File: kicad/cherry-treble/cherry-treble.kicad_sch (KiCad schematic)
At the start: 103 parts

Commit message: Pick compatible PCB components for cherry trebble
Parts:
- Conn1: footprint Connector_Multicomp:Multicomp_MC9A12-2634_2x13_P2.54mm_Vertical -> Connector_IDC:IDC-Header_2x13_P2.54mm_Vertical
- R0, R1, R2, R3, R4, R5: footprint Resistor_SMD:R_1206_3216Metric_Pad1.42x1.75mm_HandSolder -> Resistor_SMD:R_1206_3216Metric_Pad1.30x1.75mm_HandSolder
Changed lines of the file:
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@@
       (effects (font (size 1.27 1.27)) (justify left))
     )
-    (property "Footprint" "Resistor_SMD:R_1206_3216Metric_Pad1.42x1.75mm_HandSolder" (id 2) (at 153.67 155.448 90)
+    (property "Footprint" "Resistor_SMD:R_1206_3216Metric_Pad1.30x1.75mm_HandSolder" (id 2) (at 153.67 155.448 90)
       (effects (font (size 1.27 1.27)) hide)
     )
@@
       (effects (font (size 1.27 1.27)) (justify left))
     )
-    (property "Footprint" "Resistor_SMD:R_1206_3216Metric_Pad1.42x1.75mm_HandSolder" (id 2) (at 153.67 133.858 90)
+    (property "Footprint" "Resistor_SMD:R_1206_3216Metric_Pad1.30x1.75mm_HandSolder" (id 2) (at 153.67 133.858 90)
       (effects (font (size 1.27 1.27)) hide)
     )
@@
       (effects (font (size 1.27 1.27)) (justify left))
     )
-    (property "Footprint" "Resistor_SMD:R_1206_3216Metric_Pad1.42x1.75mm_HandSolder" (id 2) (at 153.67 112.268 90)
+    (property "Footprint" "Resistor_SMD:R_1206_3216Metric_Pad1.30x1.75mm_HandSolder" (id 2) (at 153.67 112.268 90)
       (effects (font (size 1.27 1.27)) hide)
     )
@@
     (property "Reference" "Conn1" (id 0) (at 190.5 17.3482 0))
     (property "Value" "Conn_02x13_Odd_Even" (id 1) (at 190.5 19.6596 0))
-    (property "Footprint" "Connector_Multicomp:Multicomp_MC9A12-2634_2x13_P2.54mm_Vertical" (id 2) (at 189.23 38.1 0)
+    (property "Footprint" "Connector_IDC:IDC-Header_2x13_P2.54mm_Vertical" (id 2) (at 189.23 38.1 0)
       (effects (font (size 1.27 1.27)) hide)
     )
@@
       (effects (font (size 1.27 1.27)) (justify left))
     )
-    (property "Footprint" "Resistor_SMD:R_1206_3216Metric_Pad1.42x1.75mm_HandSolder" (id 2) (at 153.67 90.678 90)
+    (property "Footprint" "Resistor_SMD:R_1206_3216Metric_Pad1.30x1.75mm_HandSolder" (id 2) (at 153.67 90.678 90)
       (effects (font (size 1.27 1.27)) hide)
     )
@@
       (effects (font (size 1.27 1.27)) (justify left))
     )
-    (property "Footprint" "Resistor_SMD:R_1206_3216Metric_Pad1.42x1.75mm_HandSolder" (id 2) (at 153.67 69.088 90)
+    (property "Footprint" "Resistor_SMD:R_1206_3216Metric_Pad1.30x1.75mm_HandSolder" (id 2) (at 153.67 69.088 90)
       (effects (font (size 1.27 1.27)) hide)
     )
@@
       (effects (font (size 1.27 1.27)) (justify left))
     )
-    (property "Footprint" "Resistor_SMD:R_1206_3216Metric_Pad1.42x1.75mm_HandSolder" (id 2) (at 153.67 47.498 90)
+    (property "Footprint" "Resistor_SMD:R_1206_3216Metric_Pad1.30x1.75mm_HandSolder" (id 2) (at 153.67 47.498 90)
       (effects (font (size 1.27 1.27)) hide)
     )
@@
     )
     (path "/9e3b6ef3-52a8-4dd9-a8f4-b7171c5fee3c"
-      (reference "Conn1") (unit 1) (value "Conn_02x13_Odd_Even") (footprint "Connector_Multicomp:Multicomp_MC9A12-2634_2x13_P2.54mm_Vertical")
+      (reference "Conn1") (unit 1) (value "Conn_02x13_Odd_Even") (footprint "Connector_IDC:IDC-Header_2x13_P2.54mm_Vertical")
     )
     (path "/97178bdc-fdcc-45db-99b3-0df4ecddfa55"
@@
     )
     (path "/cfce948b-9f72-4e81-a12b-89c726c6fcef"
-      (reference "R0") (unit 1) (value "10k") (footprint "Resistor_SMD:R_1206_3216Metric_Pad1.42x1.75mm_HandSolder")
+      (reference "R0") (unit 1) (value "10k") (footprint "Resistor_SMD:R_1206_3216Metric_Pad1.30x1.75mm_HandSolder")
     )
     (path "/bff3b85d-eb38-420c-9f5c-44f931425e43"
-      (reference "R1") (unit 1) (value "10k") (footprint "Resistor_SMD:R_1206_3216Metric_Pad1.42x1.75mm_HandSolder")
+      (reference "R1") (unit 1) (value "10k") (footprint "Resistor_SMD:R_1206_3216Metric_Pad1.30x1.75mm_HandSolder")
     )
     (path "/b5a7ad3d-c26d-4413-83db-9bfba22fa6f0"
-      (reference "R2") (unit 1) (value "10k") (footprint "Resistor_SMD:R_1206_3216Metric_Pad1.42x1.75mm_HandSolder")
+      (reference "R2") (unit 1) (value "10k") (footprint "Resistor_SMD:R_1206_3216Metric_Pad1.30x1.75mm_HandSolder")
     )
     (path "/986371c7-5271-475e-9c30-54695843300e"
-      (reference "R3") (unit 1) (value "10k") (footprint "Resistor_SMD:R_1206_3216Metric_Pad1.42x1.75mm_HandSolder")
+      (reference "R3") (unit 1) (value "10k") (footprint "Resistor_SMD:R_1206_3216Metric_Pad1.30x1.75mm_HandSolder")
     )
     (path "/5e9c7ff3-fbe3-4ba5-b51a-22b9f0fd8c94"
-      (reference "R4") (unit 1) (value "10k") (footprint "Resistor_SMD:R_1206_3216Metric_Pad1.42x1.75mm_HandSolder")
+      (reference "R4") (unit 1) (value "10k") (footprint "Resistor_SMD:R_1206_3216Metric_Pad1.30x1.75mm_HandSolder")
     )
     (path "/3ff8e6a9-719c-4bfc-af0b-9e00ac7758b8"
-      (reference "R5") (unit 1) (value "10k") (footprint "Resistor_SMD:R_1206_3216Metric_Pad1.42x1.75mm_HandSolder")
+      (reference "R5") (unit 1) (value "10k") (footprint "Resistor_SMD:R_1206_3216Metric_Pad1.30x1.75mm_HandSolder")
     )
     (path "/284fe915-29d9-4b8c-b528-5698bc79fdd4"

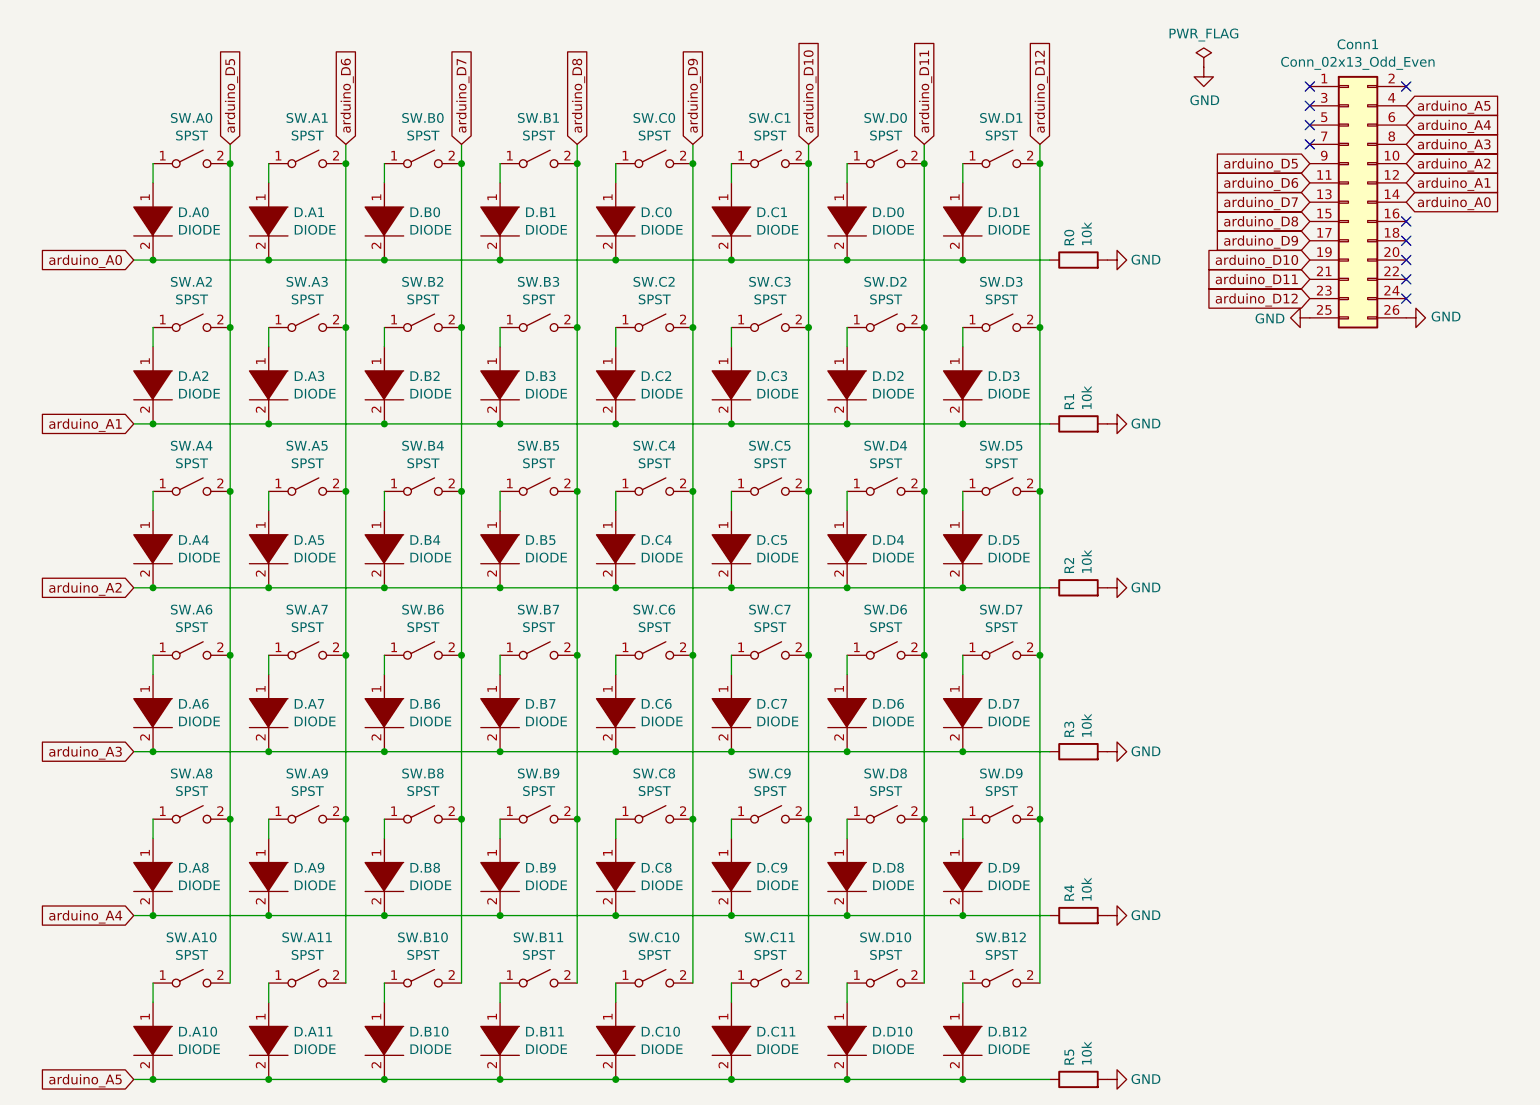
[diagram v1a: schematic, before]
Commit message: Update wiring schematic for cherry treble
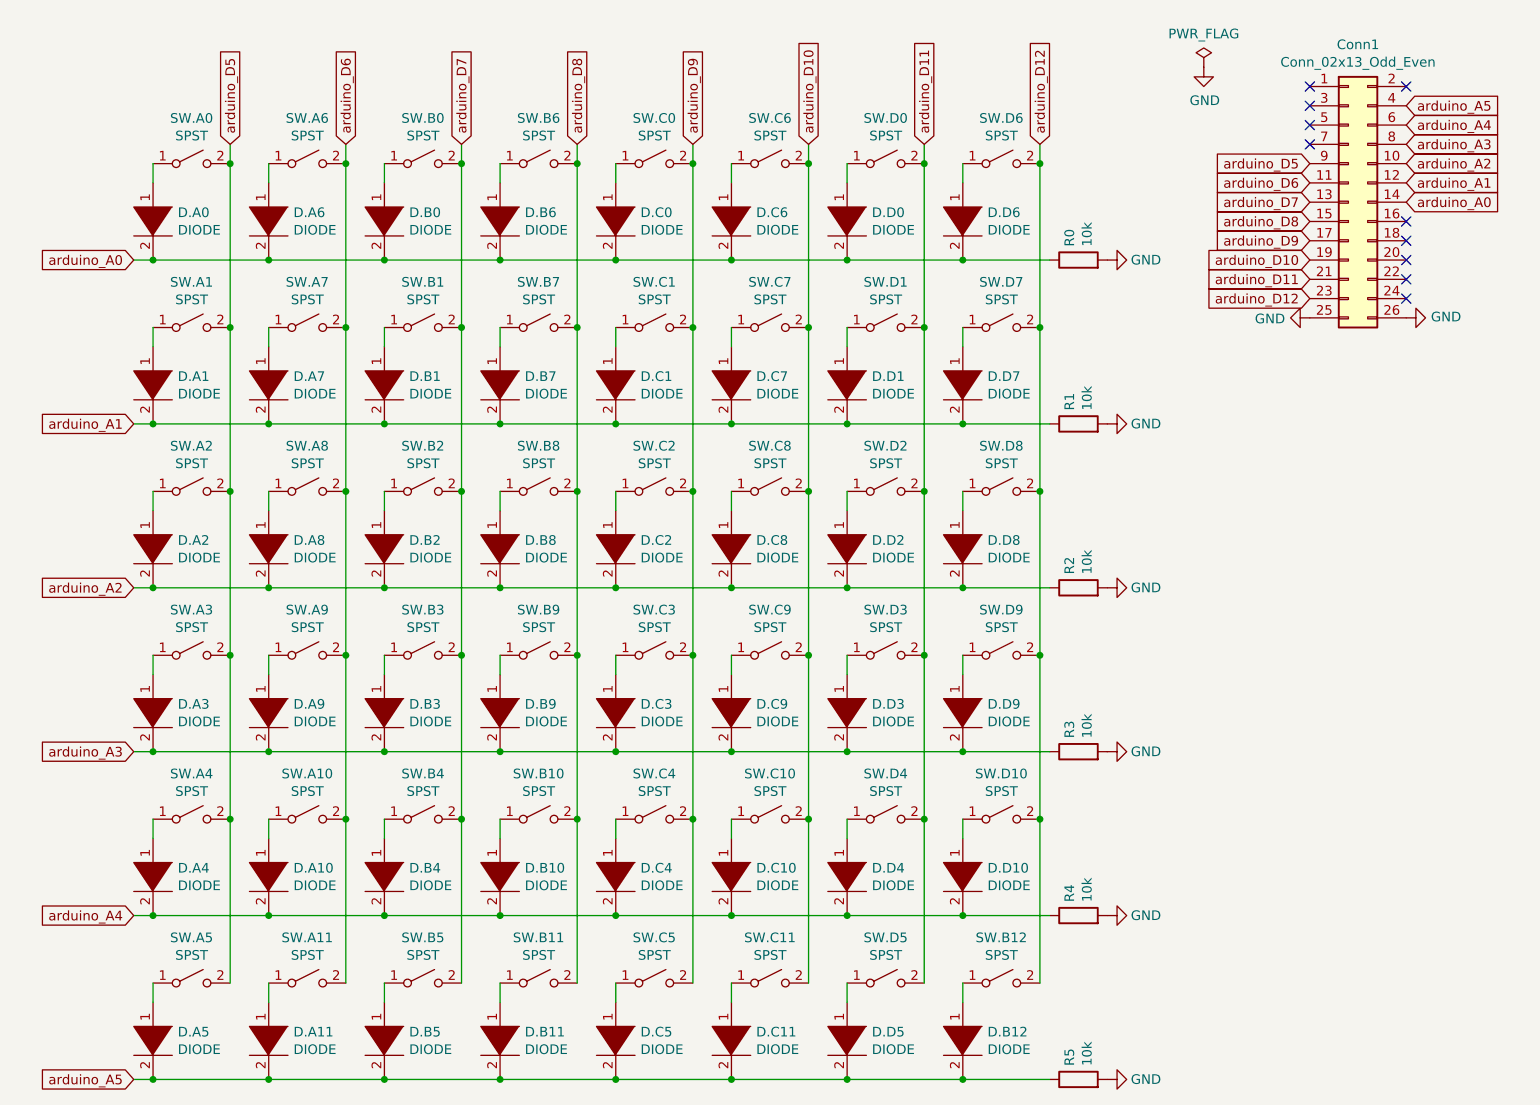
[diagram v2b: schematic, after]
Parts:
- renumbered D.A2 to D.A1, D.A9 to D.A10, D.A4 to D.A2, D.A6 to D.A3, D.A8 to D.A4, D.A10 to D.A5, D.A1 to D.A6, D.A3 to D.A7, D.A5 to D.A8, D.A7 to D.A9, D.B2 to D.B1, D.B9 to D.B10, D.B4 to D.B2, D.B6 to D.B3, D.B8 to D.B4, D.B10 to D.B5, D.B1 to D.B6, D.B3 to D.B7, D.B5 to D.B8, D.B7 to D.B9, D.C2 to D.C1, D.C9 to D.C10, D.C4 to D.C2, D.C6 to D.C3, D.C8 to D.C4, D.C10 to D.C5, D.C1 to D.C6, D.C3 to D.C7, D.C5 to D.C8, D.C7 to D.C9, D.D2 to D.D1, D.D9 to D.D10, D.D4 to D.D2, D.D6 to D.D3, D.D8 to D.D4, D.D10 to D.D5, D.D1 to D.D6, D.D3 to D.D7, D.D5 to D.D8, D.D7 to D.D9, SW.A2 to SW.A1, SW.A9 to SW.A10, SW.A4 to SW.A2, SW.A6 to SW.A3, SW.A8 to SW.A4, SW.A10 to SW.A5, SW.A1 to SW.A6, SW.A3 to SW.A7, SW.A5 to SW.A8, SW.A7 to SW.A9, SW.B2 to SW.B1, SW.B9 to SW.B10, SW.B4 to SW.B2, SW.B6 to SW.B3, SW.B8 to SW.B4, SW.B10 to SW.B5, SW.B1 to SW.B6, SW.B3 to SW.B7, SW.B5 to SW.B8, SW.B7 to SW.B9, SW.C2 to SW.C1, SW.C9 to SW.C10, SW.C4 to SW.C2, SW.C6 to SW.C3, SW.C8 to SW.C4, SW.C10 to SW.C5, SW.C1 to SW.C6, SW.C3 to SW.C7, SW.C5 to SW.C8, SW.C7 to SW.C9, SW.D2 to SW.D1, SW.D9 to SW.D10, SW.D4 to SW.D2, SW.D6 to SW.D3, SW.D8 to SW.D4, SW.D10 to SW.D5, SW.D1 to SW.D6, SW.D3 to SW.D7, SW.D5 to SW.D8, SW.D7 to SW.D9

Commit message: Exclude cherry switches from BOM
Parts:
- Conn1, SW.A0, SW.A1, SW.A10, SW.A11, SW.A2, SW.A3, SW.A4, SW.A5, SW.A6, SW.A7, SW.A8, SW.A9, SW.B0, SW.B1, SW.B10, SW.B11, SW.B12, SW.B2, SW.B3, SW.B4, SW.B5, SW.B6, SW.B7, SW.B8, SW.B9, SW.C0, SW.C1, SW.C10, SW.C11, SW.C2, SW.C3, SW.C4, SW.C5, SW.C6, SW.C7, SW.C8, SW.C9, SW.D0, SW.D1, SW.D10, SW.D2, SW.D3, SW.D4, SW.D5, SW.D6, SW.D7, SW.D8, SW.D9: now left out of the parts list

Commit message: Name the diodes on cherry treble
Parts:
- D.A0, D.A1, D.A10, D.A11, D.A2, D.A3, D.A4, D.A5, D.A6, D.A7, D.A8, D.A9, D.B0, D.B1, D.B10, D.B11, D.B12, D.B2, D.B3, D.B4, D.B5, D.B6, D.B7, D.B8, D.B9, D.C0, D.C1, D.C10, D.C11, D.C2, D.C3, D.C4, D.C5, D.C6, D.C7, D.C8, D.C9, D.D0, D.D1, D.D10, D.D2, D.D3, D.D4, D.D5, D.D6, D.D7, D.D8, D.D9: value DIODE -> 1N4148WS

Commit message: Add part numbers for resistors in cherry treble schematics
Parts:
- R0, R1, R2, R3, R4, R5: LCSC Part # (none) -> C17902
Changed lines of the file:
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@@
+      (effects (font (size 1.27 1.27)) hide)
+    )
+    (property "LCSC Part #" "C17902" (id 4) (at 153.67 153.67 0)
       (effects (font (size 1.27 1.27)) hide)
     )
@@
       (effects (font (size 1.27 1.27)) hide)
     )
+    (property "LCSC Part #" "C17902" (id 4) (at 153.67 132.08 0)
+      (effects (font (size 1.27 1.27)) hide)
+    )
     (pin "1")
     (pin "2")
@@
     )
     (property "Datasheet" "~" (id 3) (at 153.67 110.49 0)
+      (effects (font (size 1.27 1.27)) hide)
+    )
+    (property "LCSC Part #" "C17902" (id 4) (at 153.67 110.49 0)
       (effects (font (size 1.27 1.27)) hide)
     )
@@
       (effects (font (size 1.27 1.27)) hide)
     )
+    (property "LCSC Part #" "C17902" (id 4) (at 153.67 88.9 0)
+      (effects (font (size 1.27 1.27)) hide)
+    )
     (pin "1")
     (pin "2")
@@
       (effects (font (size 1.27 1.27)) hide)
     )
+    (property "LCSC Part #" "C17902" (id 4) (at 153.67 67.31 0)
+      (effects (font (size 1.27 1.27)) hide)
+    )
     (pin "1")
     (pin "2")
@@
       (effects (font (size 1.27 1.27)) hide)
     )
+    (property "LCSC Part #" "C17902" (id 4) (at 153.67 45.72 0)
+      (effects (font (size 1.27 1.27)) hide)
+    )
